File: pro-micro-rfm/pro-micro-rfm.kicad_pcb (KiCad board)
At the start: 2 copper layers, 44.7 x 50.8 mm, 6 parts, among them U1 ProMicro, U2 AP1117, U3 RFM69

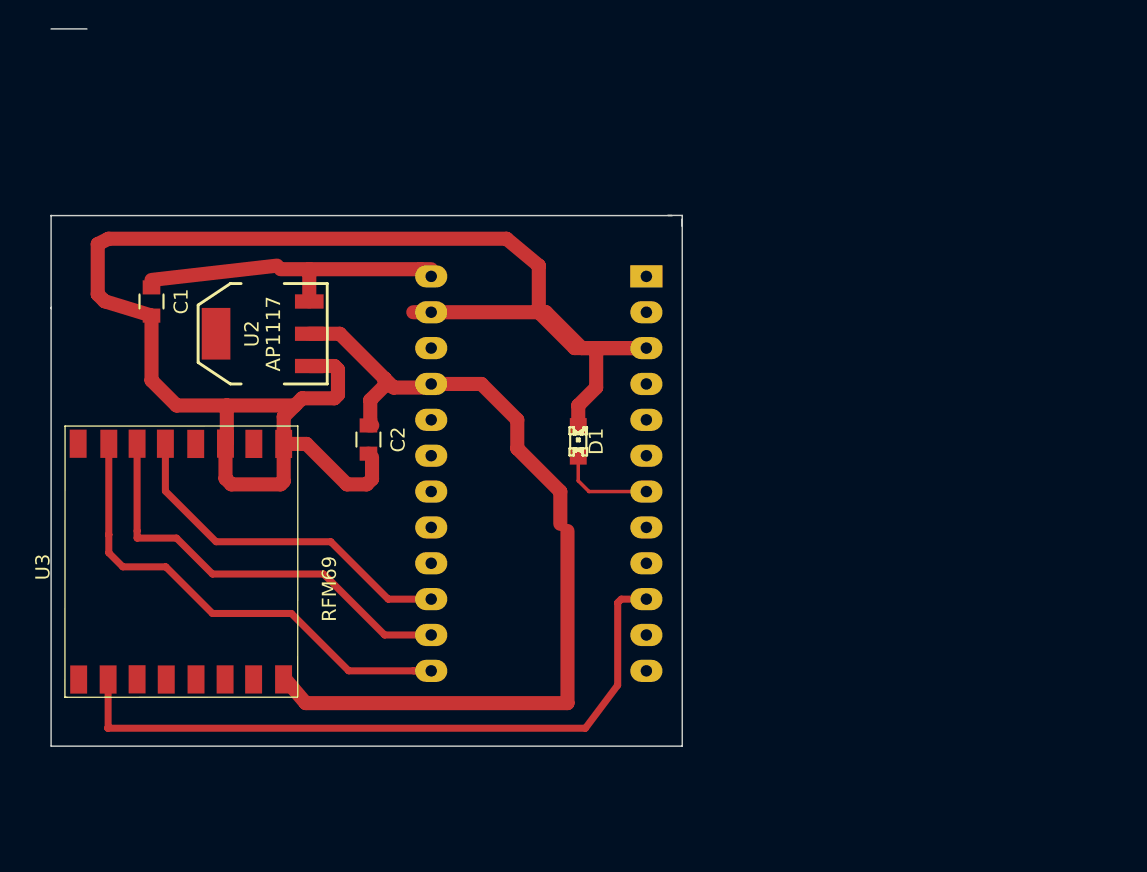
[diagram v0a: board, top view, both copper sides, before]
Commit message: minor pcb edits misssed sck line
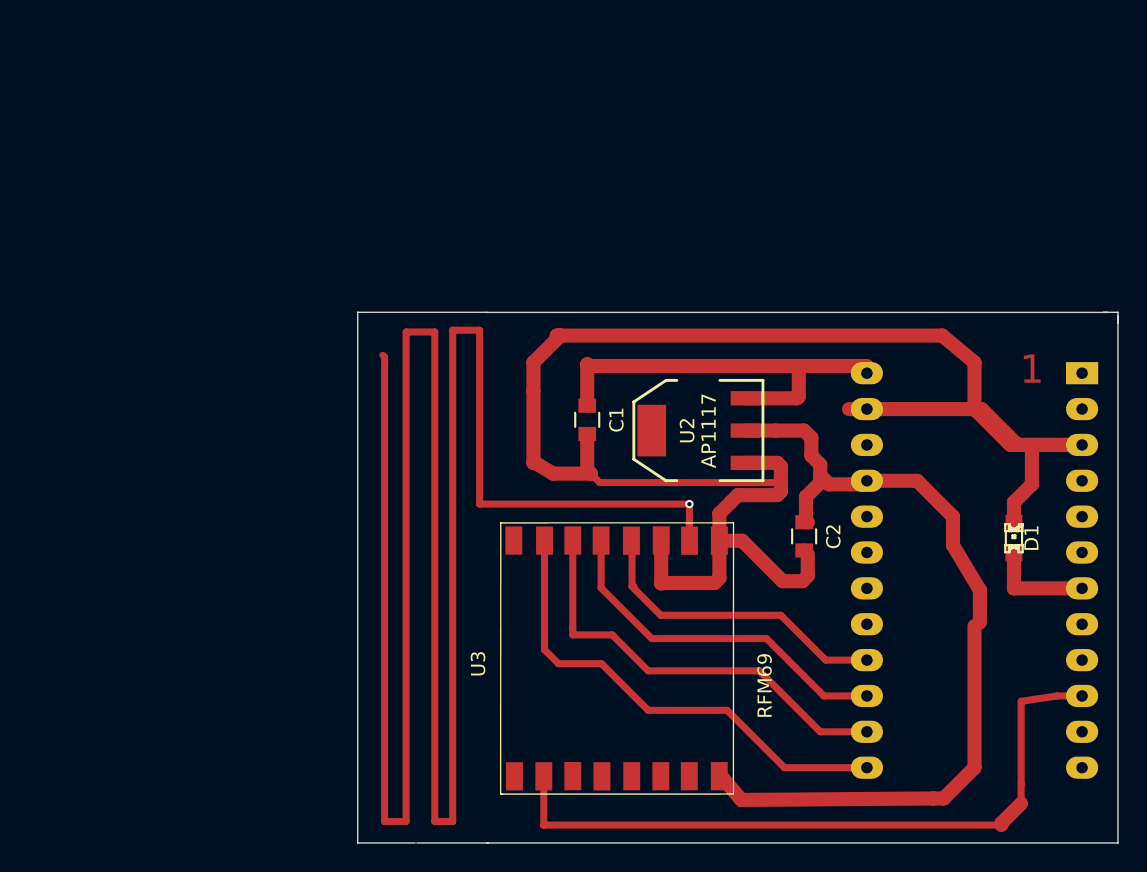
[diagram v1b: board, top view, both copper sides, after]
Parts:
- moved C1 32.0 mm to (71.0, 45.5)
- moved U1 31.6 mm to (102.2, 56.1)
- moved U2 31.6 mm to (78.9, 46.2)
- moved C2 31.6 mm to (86.4, 53.7)
- moved U3 31.6 mm to (74.0, 62.7)
- moved D1 31.6 mm to (101.2, 53.8)
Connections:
- U1 pad 1: (no net) -> Net-(U1-Pad1)
- U1 pad 11: (no net) -> Net-(U1-Pad11)
- U1 pad 12: (no net) -> Net-(U1-Pad12)
- U1 pad 16: (no net) -> Net-(U1-Pad16)
- U1 pad 17: (no net) -> Net-(U1-Pad17)
- U1 pad 18: (no net) -> Net-(U1-Pad18)
- U1 pad 19: (no net) -> Net-(U1-Pad19)
- U1 pad 2: (no net) -> Net-(U1-Pad2)
- U1 pad 20: (no net) -> Net-(U1-Pad20)
- U1 pad 22: (no net) -> Net-(U1-Pad22)
- U1 pad 4: (no net) -> Net-(U1-Pad4)
- U1 pad 5: (no net) -> Net-(U1-Pad5)
- U1 pad 6: (no net) -> Net-(U1-Pad6)
- U1 pad 8: (no net) -> Net-(U1-Pad8)
- U1 pad 9: (no net) -> Net-(U1-Pad9)
- U3 pad 1: (no net) -> Net-(U3-Pad1)
- U3 pad 10: (no net) -> Net-(U3-Pad10)
- U3 pad 12: (no net) -> Net-(U1-Pad16)
- U3 pad 16: (no net) -> Net-(U3-Pad16)
- U3 pad 3: (no net) -> Net-(U3-Pad3)
- U3 pad 4: (no net) -> Net-(U3-Pad4)
- U3 pad 5: (no net) -> Net-(U3-Pad5)
- U3 pad 6: (no net) -> Net-(U3-Pad6)
- U3 pad 7: (no net) -> Net-(U3-Pad7)
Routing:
- net Net-(U3-Pad10): track 0.00 -> 173.7 mm, vias 0 -> 1
- net Net-(U1-Pad16): track 0.00 -> 22.1 mm
- net Net-(C1-Pad1): track 23.3 -> 31.7 mm
- net GND: track 122.9 -> 128.0 mm
- net Net-(C2-Pad1): track 64.3 -> 61.4 mm
- net Net-(U1-Pad10): track 49.1 -> 49.6 mm
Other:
- board size 44.7 x 50.8 mm -> 53.8 x 37.6 mm
- board text added: "1"
